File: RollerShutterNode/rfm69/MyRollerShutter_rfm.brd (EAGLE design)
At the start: 47 x 47.9 mm, 51 parts, among them IC1 ATMega-328, IC2 AT25DF512C-SSHN-B, IC3 MCP1703CB, IC4 ACS712_5A, IC5 ATSHA204A, IC6 LM321, IC7 MDC3105DMT1, X1 8 MHz

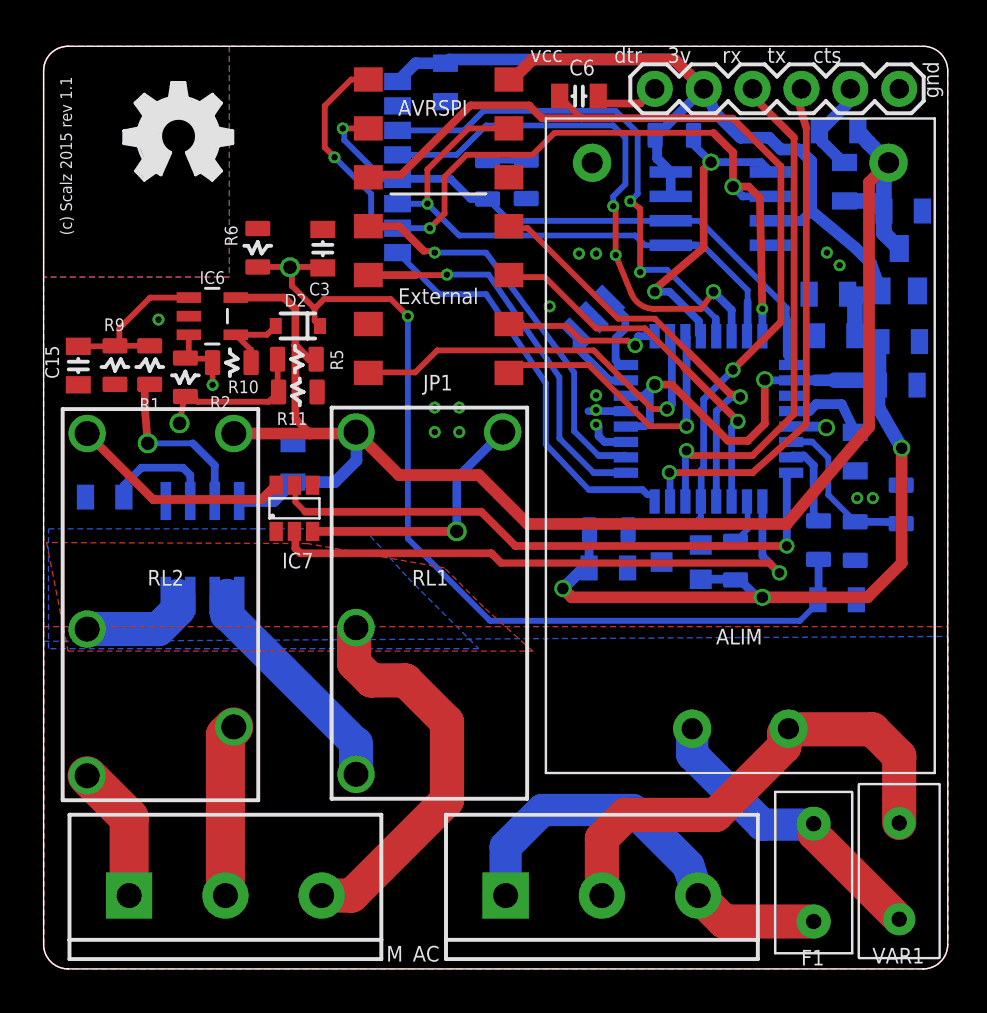
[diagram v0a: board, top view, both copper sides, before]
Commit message: some rerouting and a small fix on connector
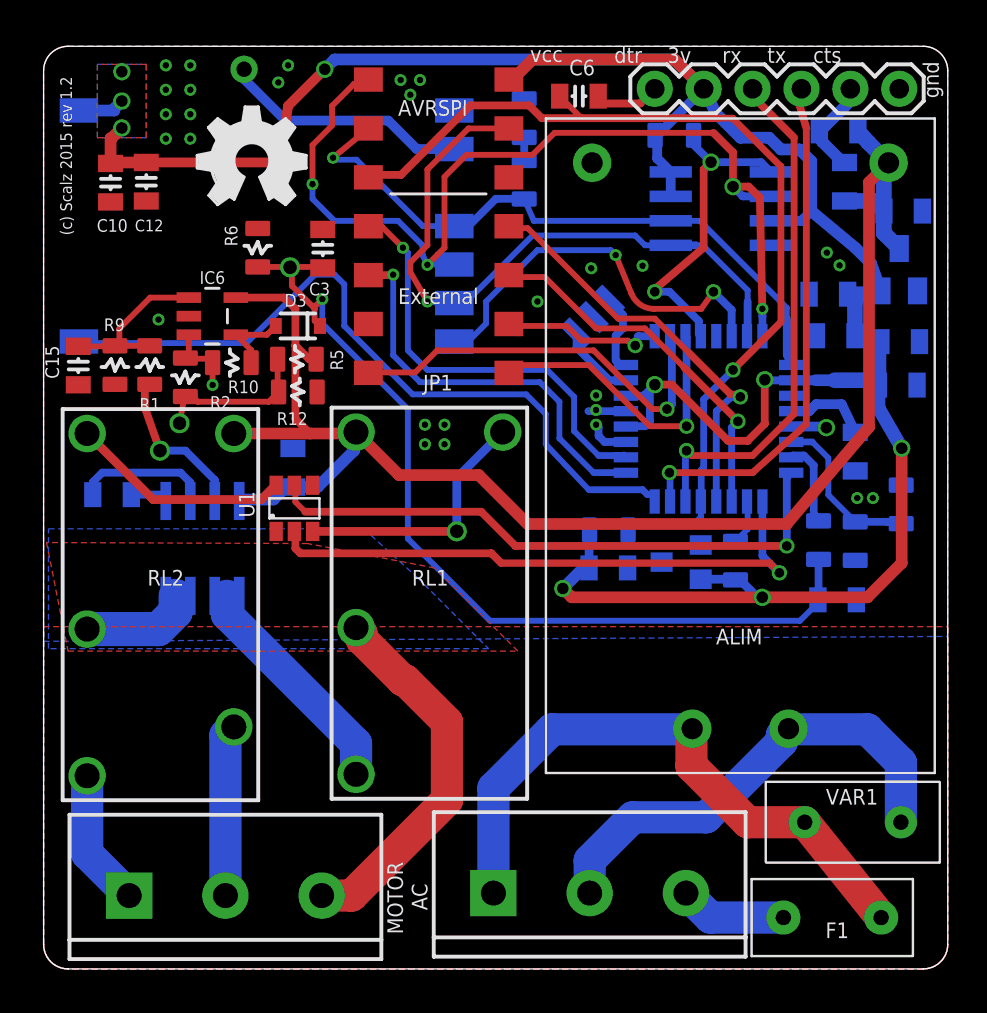
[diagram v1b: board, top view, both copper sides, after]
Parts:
- removed D1: LED0805, LowPowerLab:0805-LED
- removed NRF_SMD: NRF24L01+SMD_MODULE, pmo_lib:NRF24L01+SMD_MODULE
- removed R11: (no value), LowPowerLab:0805-RES
- added ANT: RFM12B_ANTENNA, LowPowerLab:RFM12B-ANTENNA
- added C17: 0.1u, LowPowerLab:0805-CAP
- added D4: LED0805, LowPowerLab:0805-LED
- added R14: 1k5, LowPowerLab:0805-RES
- added RFM69: RFM69, LowPowerLab:RFM69W-MINPADS
- R12: value 1k5 -> (none)
- moved C12 35.9 mm to (5.33, 40.9), flipped to the top, turned to 90 degrees
- moved C10 18.2 mm to (3.48, 40.8), flipped to the top
- moved R12 14.8 mm to (13.2, 30.0), flipped to the top, turned to 180 degrees
- moved U$4 4.02 mm to (7.98, 39.7)
- moved VAR1 3.50 mm to (42.0, 7.62), turned to 180 degrees
- moved F1 2.53 mm to (41.0, 2.67), turned to 0 degrees
- moved AC 0.65 mm to (23.4, 3.94)
- moved C2 0.40 mm to (3.56, 24.6), turned to 180 degrees
- moved C1 0.25 mm to (13.0, 26.0)
- renumbered D2 to D3, IC7 to U1, M to MOTOR, R13 to R21
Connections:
- net COM renamed OUT_ACS
- net NEUTRE renamed N
- net TOGGLE renamed IN_ACS
- new net N$4: ANT.P$1, RFM69.ANA
- net D2: now also RFM69.DIO0; no longer NRF_SMD.IRQ
- net D9: no longer NRF_SMD.CE
- net GND: now also C12.1, C17.2, D4.MINUS, R12.1, RFM69.GND; no longer C12.2, D1.MINUS, NRF_SMD.GND, R11.1
- net L: no longer AC.1
- net MISO: now also RFM69.MISO; no longer NRF_SMD.MISO
- net MOSI: now also RFM69.MOSI; no longer NRF_SMD.MOSI
- net N$17: now also D4.PLUS, R14.2; no longer D1.PLUS, R12.2
- net N$18: now also R12.2; no longer R11.2
- net PHASE: now also AC.1
- net RF_CSN: now also RFM69.NSS; no longer NRF_SMD.CSN
- net SCK: now also R14.1, RFM69.SCK; no longer NRF_SMD.SCK, R12.1
- net VCC: now also C12.2, C17.1, RFM69.VDD; no longer C12.1, NRF_SMD.3V
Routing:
- net D9: track 27.0 -> 0.03 mm, vias 2 -> 0
- net VCC: track 119.6 -> 142.0 mm, vias 5 -> 9
- net D2: track 21.5 -> 38.7 mm
- net L: track 22.2 -> 5.59 mm
- net PHASE: track 16.0 -> 32.5 mm
- net N$4: track 0.00 -> 12.9 mm
- net RF_CSN: track 29.0 -> 21.0 mm, vias 3 -> 2
- net MISO: track 45.0 -> 51.0 mm
- net MOSI: track 29.3 -> 34.3 mm
- net GND: track 11.2 -> 13.3 mm, vias 16 -> 29
- net A0: track 49.8 -> 47.8 mm
- net SCK: track 31.7 -> 33.7 mm
- net D4: track 20.7 -> 22.4 mm
- net D3: track 20.1 -> 21.4 mm
- net N$1: track 5.94 -> 7.09 mm
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- added copper zone on layer 1, net VCC
- added copper zone on layer 16, net VCC
- removed copper zone on layer 1, net N$14
- removed copper zone on layer 16, net N$15
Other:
- board text added: "(c) Scalz 2015 rev 1.2"
- board text removed: "(c) Scalz 2015 rev 1.1"
